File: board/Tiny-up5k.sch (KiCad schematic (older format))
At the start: 37 parts, among them J1 CONN_01X14, J2 CONN_01X14, J5 Prog, SW1 SW_Push, U1 ICE40UP5K-SG48ITR, U2 MIC5504-3.3YM5, U3 DSC6001CI2A-016.0000T, U4 MIC5504-1.2YM5, U5 AT25xxx-MA, U6 USB_OTG

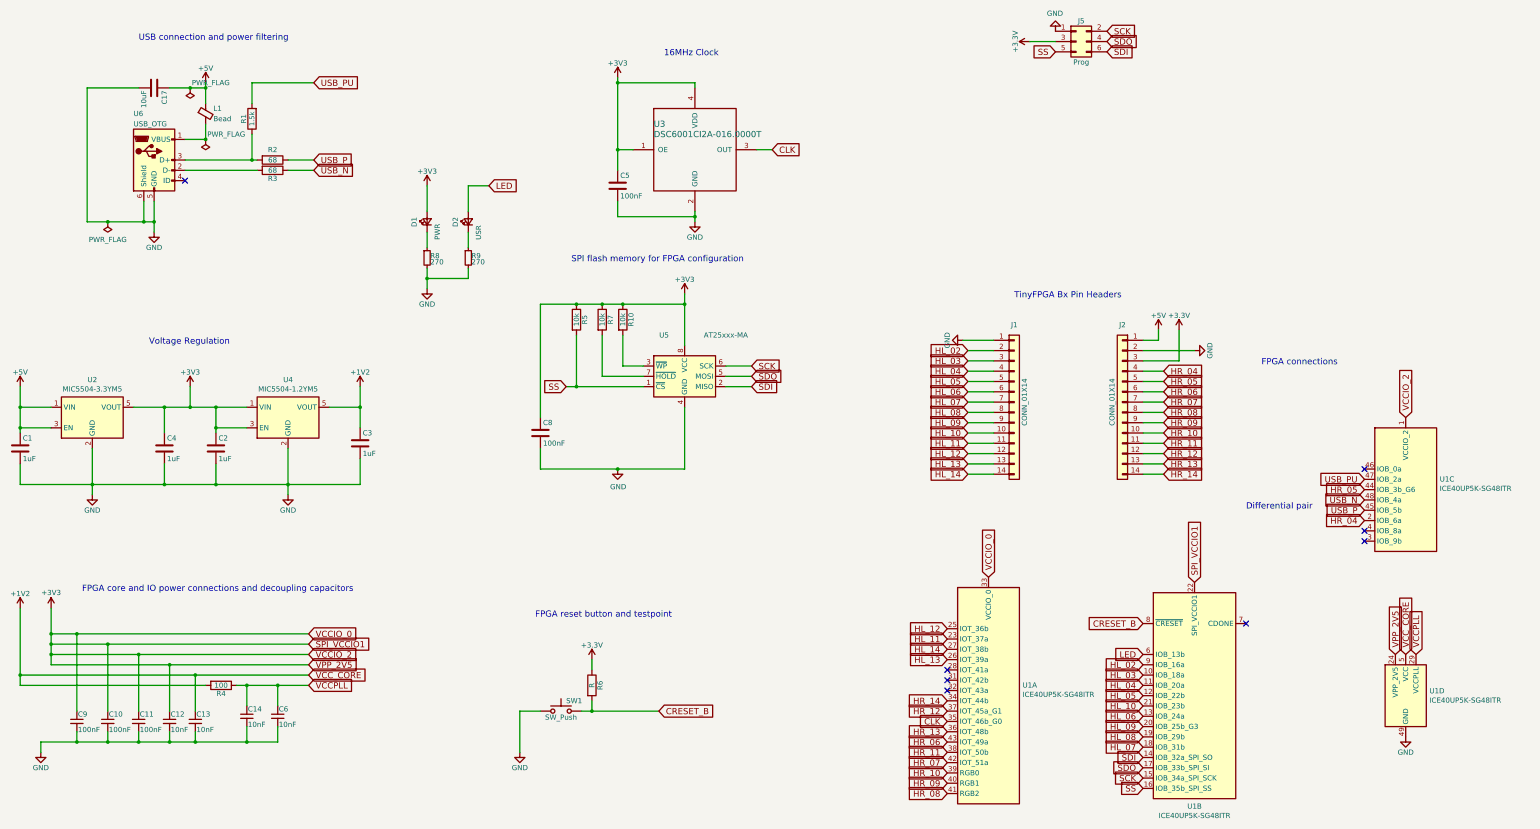
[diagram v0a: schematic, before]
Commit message: Added more part numbers for the components. Changed the footprint of 5v capacitor (make it bigger) to accomodate for the bigger value.
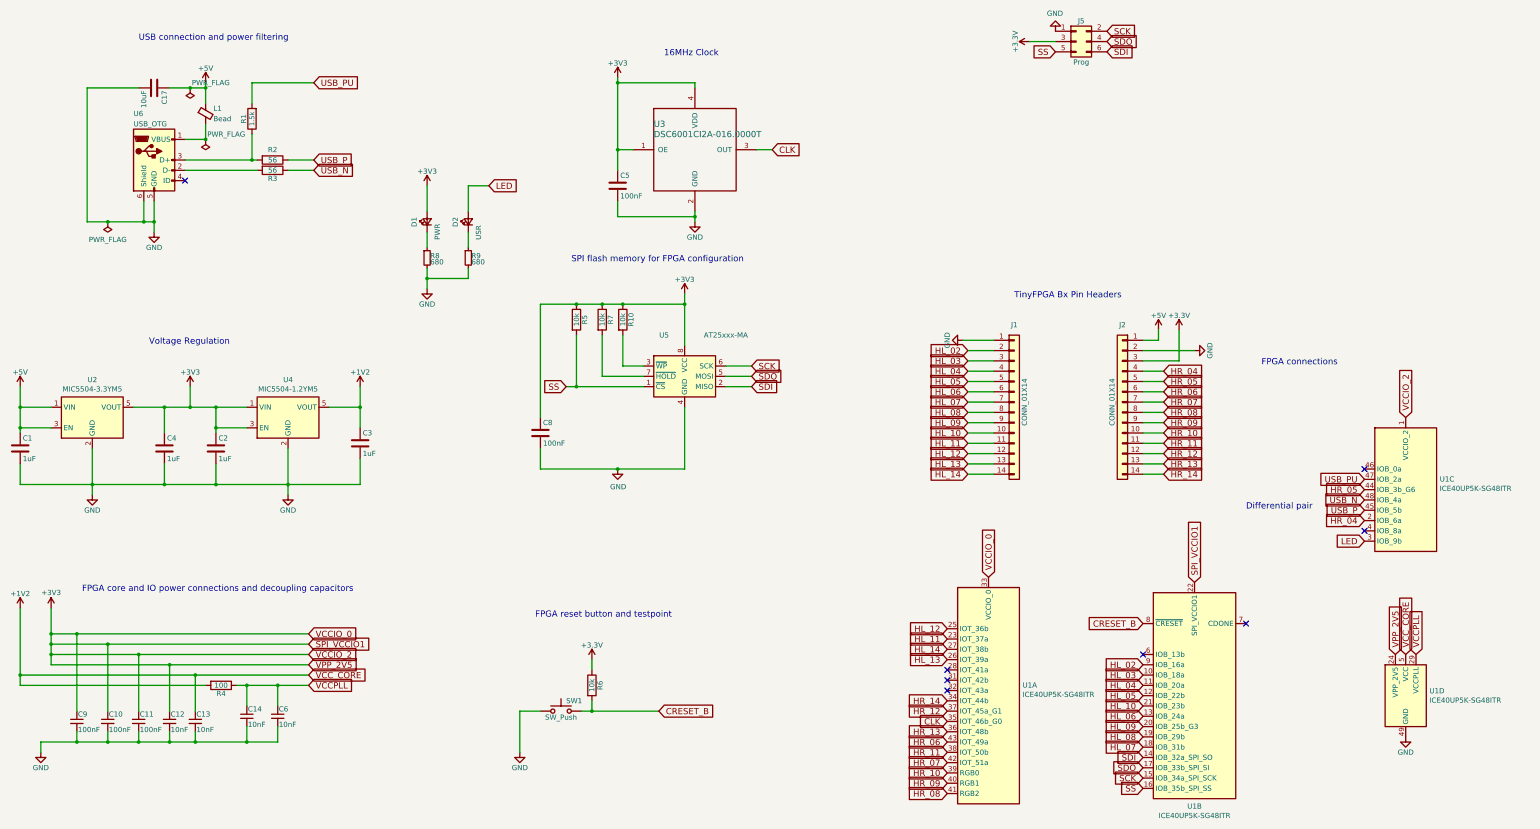
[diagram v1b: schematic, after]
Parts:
- C1, C2, C3, C4: manf# (none) -> GRM155R61A105KE15D
- C10, C11, C5, C8, C9: manf# (none) -> GRM155R71A104KA01D
- C12, C13, C14, C6: manf# (none) -> GRM155R61A103KA01D
- C17: footprint Capacitor_SMD:C_0402_1005Metric -> Capacitor_SMD:C_0603_1608Metric; manf# (none) -> GRM188R61A106KE69D
- D1, D2: manf# (none) -> KPHD-1608LVCGCK
- L1: manf# (none) -> BLM18PG300SN1D
- R1: footprint Resistors_SMD:R_0402_NoSilk -> Resistor_SMD:R_0402_1005Metric; manf# (none) -> CRCW04021K50FKED
- R10, R5, R7: footprint Resistors_SMD:R_0402_NoSilk -> Resistor_SMD:R_0402_1005Metric; manf# (none) -> CRCW040210K0FKED
- R2, R3: value 68 -> 56; footprint Resistors_SMD:R_0402_NoSilk -> Resistor_SMD:R_0402_1005Metric; manf# (none) -> CRCW040256R0FKED
- R4: footprint Resistors_SMD:R_0402_NoSilk -> Resistor_SMD:R_0402_1005Metric; manf# (none) -> CRCW0402100RFKED
- R6: value R -> 10k; footprint Resistors_SMD:R_0402 -> Resistor_SMD:R_0402_1005Metric; manf# (none) -> CRCW040210K0FKED
- R8, R9: value 270 -> 680; footprint Resistors_SMD:R_0402_NoSilk -> Resistor_SMD:R_0402_1005Metric; manf# (none) -> CRCW0402680RFKED
- U2: manf# MIC5504-3.3YM5-TR -> MIC5504-3.3YM5-TR
- U5: #manf AT25SF081-MHD-T -> (none); manf# (none) -> AT25SF081-MHD-T
- U6: manf# USB3076-30-A -> USB3076-30-A
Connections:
- net LED: now also U1.3 (IOB_9b); no longer U1.6 (IOB_13b)
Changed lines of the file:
@@
 encoding utf-8
 Sheet 1 1
-Title "TinyFPGA Bx"
+Title "Tiny-up5k"
 Date ""
 Rev "v1.1"
-Comp "TinyFPGA"
+Comp "Not Organized"
 Comment1 ""
 Comment2 ""
@@
 F 2 "Connector_USB:USB_Micro-B_GCT_USB3076-30-A" H 2350 1950 50  0001 C CNN
 F 3 "" H 2350 1950 50  0001 C CNN
-F 4 "USB3076-30-A " H 2200 2000 50  0001 C CNN "manf#"
+F 4 "USB3076-30-A" H 2200 2000 50  0001 C CNN "manf#"
 	1    2200 2000
 	1    0    0    -1
@@
 F 2 "Capacitor_SMD:C_0402_1005Metric" H 2838 4650 50  0001 C CNN
 F 3 "" H 2800 4800 50  0001 C CNN
+F 4 "GRM155R61A105KE15D" H 0   0   50  0001 C CNN "manf#"
 	1    2800 4800
 	1    0    0    -1
@@
 F 2 "Capacitor_SMD:C_0402_1005Metric" H 4238 4600 50  0001 C CNN
 F 3 "" H 4200 4750 50  0001 C CNN
+F 4 "GRM155R61A105KE15D" H 0   0   50  0001 C CNN "manf#"
 	1    4200 4750
 	1    0    0    -1
@@
 F 2 "Capacitor_SMD:C_0402_1005Metric" H 938 4650 50  0001 C CNN
 F 3 "" H 900 4800 50  0001 C CNN
+F 4 "GRM155R61A105KE15D" H 0   0   50  0001 C CNN "manf#"
 	1    900  4800
 	1    0    0    -1
@@
 F 2 "Capacitor_SMD:C_0402_1005Metric" H 2338 4650 50  0001 C CNN
 F 3 "" H 2300 4800 50  0001 C CNN
+F 4 "GRM155R61A105KE15D" H 0   0   50  0001 C CNN "manf#"
 	1    2300 4800
 	1    0    0    -1
@@
 F 2 "Inductors_SMD:L_0603" V 2630 1550 50  0001 C CNN
 F 3 "" H 2700 1550 50  0001 C CNN
+F 4 "BLM18PG300SN1D" H 2700 1550 50  0001 C CNN "manf#"
 	1    2700 1550
 	1    0    0    -1
@@
 P 3350 2000
 F 0 "R2" V 3250 2000 50  0000 C CNN
-F 1 "68" V 3350 2000 50  0000 C CNN
-F 2 "Resistors_SMD:R_0402_NoSilk" V 3280 2000 50  0001 C CNN
+F 1 "56" V 3350 2000 50  0000 C CNN
+F 2 "Resistor_SMD:R_0402_1005Metric" V 3280 2000 50  0001 C CNN
 F 3 "" H 3350 2000 50  0001 C CNN
+F 4 "CRCW040256R0FKED" H 0   0   50  0001 C CNN "manf#"
 	1    3350 2000
 	0    1    1    0
@@
 P 3350 2100
 F 0 "R3" V 3430 2100 50  0000 C CNN
-F 1 "68" V 3350 2100 50  0000 C CNN
-F 2 "Resistors_SMD:R_0402_NoSilk" V 3280 2100 50  0001 C CNN
+F 1 "56" V 3350 2100 50  0000 C CNN
+F 2 "Resistor_SMD:R_0402_1005Metric" V 3280 2100 50  0001 C CNN
 F 3 "" H 3350 2100 50  0001 C CNN
+F 4 "CRCW040256R0FKED" H 0   0   50  0001 C CNN "manf#"
 	1    3350 2100
 	0    1    1    0
@@
 F 0 "R1" V 3230 1600 50  0000 C CNN
 F 1 "1.5k" V 3150 1600 47  0000 C CNN
-F 2 "Resistors_SMD:R_0402_NoSilk" V 3080 1600 50  0001 C CNN
+F 2 "Resistor_SMD:R_0402_1005Metric" V 3080 1600 50  0001 C CNN
 F 3 "" H 3150 1600 50  0001 C CNN
+F 4 "CRCW04021K50FKED" H 0   0   50  0001 C CNN "manf#"
 	1    3150 1600
 	-1   0    0    1
@@
 F 2 "Capacitor_SMD:C_0402_1005Metric" H 6738 2100 50  0001 C CNN
 F 3 "" H 6700 2250 50  0001 C CNN
+F 4 "GRM155R71A104KA01D" H 0   0   50  0001 C CNN "manf#"
 	1    6700 2250
 	1    0    0    -1
@@
 F 2 "Capacitor_SMD:C_0402_1005Metric" H 5988 4500 50  0001 C CNN
 F 3 "" H 5950 4650 50  0001 C CNN
+F 4 "GRM155R71A104KA01D" H 0   0   50  0001 C CNN "manf#"
 	1    5950 4650
 	1    0    0    -1
@@
 F 2 "Capacitor_SMD:C_0402_1005Metric" H 1450 7450 50  0001 C CNN
 F 3 "" H 1450 7450 50  0001 C CNN
+F 4 "GRM155R71A104KA01D" H 0   0   50  0001 C CNN "manf#"
 	1    1450 7450
 	1    0    0    -1
@@
 F 2 "Capacitor_SMD:C_0402_1005Metric" H 1750 7450 50  0001 C CNN
 F 3 "" H 1750 7450 50  0001 C CNN
+F 4 "GRM155R71A104KA01D" H 0   0   50  0001 C CNN "manf#"
 	1    1750 7450
 	1    0    0    -1
@@
 F 2 "Capacitor_SMD:C_0402_1005Metric" H 2050 7450 50  0001 C CNN
 F 3 "" H 2050 7450 50  0001 C CNN
+F 4 "GRM155R71A104KA01D" H 0   0   50  0001 C CNN "manf#"
 	1    2050 7450
 	1    0    0    -1
@@
 F 2 "Capacitor_SMD:C_0402_1005Metric" H 2350 7450 50  0001 C CNN
 F 3 "" H 2350 7450 50  0001 C CNN
+F 4 "GRM155R61A103KA01D" H 0   0   50  0001 C CNN "manf#"
 	1    2350 7450
 	1    0    0    -1
@@
 F 2 "Capacitor_SMD:C_0402_1005Metric" H 2600 7450 50  0001 C CNN
 F 3 "" H 2600 7450 50  0001 C CNN
+F 4 "GRM155R61A103KA01D" H 0   0   50  0001 C CNN "manf#"
 	1    2600 7450
 	1    0    0    -1
@@
 F 2 "Capacitor_SMD:C_0402_1005Metric" H 3100 7400 50  0001 C CNN
 F 3 "" H 3100 7400 50  0001 C CNN
+F 4 "GRM155R61A103KA01D" H 0   0   50  0001 C CNN "manf#"
 	1    3100 7400
 	1    0    0    -1
@@
 F 0 "R5" V 6380 3550 50  0000 C CNN
 F 1 "10k" V 6300 3550 50  0000 C CNN
-F 2 "Resistors_SMD:R_0402_NoSilk" V 6230 3550 50  0001 C CNN
+F 2 "Resistor_SMD:R_0402_1005Metric" V 6230 3550 50  0001 C CNN
 F 3 "" H 6300 3550 50  0001 C CNN
+F 4 "CRCW040210K0FKED" H 0   0   50  0001 C CNN "manf#"
 	1    6300 3550
 	1    0    0    -1
@@
 P 6450 7100
 F 0 "R6" V 6530 7100 50  0000 C CNN
-F 1 "R" V 6450 7100 50  0000 C CNN
-F 2 "Resistors_SMD:R_0402" V 6380 7100 50  0001 C CNN
+F 1 "10k" V 6450 7100 50  0000 C CNN
+F 2 "Resistor_SMD:R_0402_1005Metric" V 6380 7100 50  0001 C CNN
 F 3 "" H 6450 7100 50  0001 C CNN
+F 4 "CRCW040210K0FKED" H 0   0   50  0001 C CNN "manf#"
 	1    6450 7100
 	1    0    0    -1
@@
 F 0 "C17" H 2225 1400 50  0000 L CNN
 F 1 "10uF" H 2225 1200 50  0000 L CNN
-F 2 "Capacitor_SMD:C_0402_1005Metric" H 2238 1150 50  0001 C CNN
+F 2 "Capacitor_SMD:C_0603_1608Metric" H 2238 1150 50  0001 C CNN
 F 3 "" H 2200 1300 50  0001 C CNN
+F 4 "GRM188R61A106KE69D" H 0   0   50  0001 C CNN "manf#"
 	1    2200 1300
 	0    1    1    0
@@
 F 0 "R7" V 6630 3550 50  0000 C CNN
 F 1 "10k" V 6550 3550 50  0000 C CNN
-F 2 "Resistors_SMD:R_0402_NoSilk" V 6480 3550 50  0001 C CNN
+F 2 "Resistor_SMD:R_0402_1005Metric" V 6480 3550 50  0001 C CNN
 F 3 "" H 6550 3550 50  0001 C CNN
+F 4 "CRCW040210K0FKED" H 0   0   50  0001 C CNN "manf#"
 	1    6550 3550
 	1    0    0    -1
@@
 F 2 "LED_SMD:LED_0402_1005Metric" V 4850 2600 50  0001 C CNN
 F 3 "" V 4850 2600 50  0001 C CNN
+F 4 "KPHD-1608LVCGCK" H 4850 2600 50  0001 C CNN "manf#"
 	1    4850 2600
 	0    -1   -1   0
@@
 F 2 "LED_SMD:LED_0402_1005Metric" V 5250 2600 50  0001 C CNN
 F 3 "" V 5250 2600 50  0001 C CNN
+F 4 "KPHD-1608LVCGCK" H 5250 2600 50  0001 C CNN "manf#"
 	1    5250 2600
 	0    -1   -1   0
@@
 P 4850 2950
 F 0 "R8" H 4880 2970 50  0000 L CNN
-F 1 "270" H 4880 2910 50  0000 L CNN
-F 2 "Resistors_SMD:R_0402_NoSilk" H 4850 2950 50  0001 C CNN
+F 1 "680" H 4880 2910 50  0000 L CNN
+F 2 "Resistor_SMD:R_0402_1005Metric" H 4850 2950 50  0001 C CNN
 F 3 "" H 4850 2950 50  0001 C CNN
+F 4 "CRCW0402680RFKED" H 4850 2950 50  0001 C CNN "manf#"
 	1    4850 2950
 	1    0    0    -1
@@
 P 5250 2950
 F 0 "R9" H 5280 2970 50  0000 L CNN
-F 1 "270" H 5280 2910 50  0000 L CNN
-F 2 "Resistors_SMD:R_0402_NoSilk" H 5250 2950 50  0001 C CNN
+F 1 "680" H 5280 2910 50  0000 L CNN
+F 2 "Resistor_SMD:R_0402_1005Metric" H 5250 2950 50  0001 C CNN
 F 3 "" H 5250 2950 50  0001 C CNN
+F 4 "CRCW0402680RFKED" H 5250 2950 50  0001 C CNN "manf#"
 	1    5250 2950
 	1    0    0    -1
@@
 F 0 "R10" V 6830 3550 50  0000 C CNN
 F 1 "10k" V 6750 3550 50  0000 C CNN
-F 2 "Resistors_SMD:R_0402_NoSilk" V 6680 3550 50  0001 C CNN
+F 2 "Resistor_SMD:R_0402_1005Metric" V 6680 3550 50  0001 C CNN
 F 3 "" H 6750 3550 50  0001 C CNN
+F 4 "CRCW040210K0FKED" H 0   0   50  0001 C CNN "manf#"
 	1    6750 3550
 	1    0    0    -1
@@
 F 0 "R4" V 2930 7100 50  0000 C CNN
 F 1 "100" V 2850 7100 50  0000 C CNN
-F 2 "Resistors_SMD:R_0402_NoSilk" V 2780 7100 50  0001 C CNN
+F 2 "Resistor_SMD:R_0402_1005Metric" V 2780 7100 50  0001 C CNN
 F 3 "" H 2850 7100 50  0001 C CNN
+F 4 "CRCW0402100RFKED" H 0   0   50  0001 C CNN "manf#"
 	1    2850 7100
 	0    1    1    0
@@
 F 2 "Capacitor_SMD:C_0402_1005Metric" H 3400 7400 50  0001 C CNN
 F 3 "" H 3400 7400 50  0001 C CNN
+F 4 "GRM155R61A103KA01D" H 0   0   50  0001 C CNN "manf#"
 	1    3400 7400
 	1    0    0    -1
@@
 Text Notes 12800 5400 0    60   ~ 0
 Differential pair
-Text GLabel 11800 6800 0    60   Input ~ 0
+Text GLabel 13950 5700 0    60   Input ~ 0
 LED
 Text GLabel 11450 750  2    60   Input ~ 0
@@
 F 2 "Package_TO_SOT_SMD:SOT-23-5" H 1600 4100 50  0001 C CNN
 F 3 "http://ww1.microchip.com/downloads/en/DeviceDoc/MIC550X.pdf" H 1350 4750 50  0001 C CNN
-F 4 " MIC5504-3.3YM5-TR" H 1600 4500 50  0001 C CNN "manf#"
+F 4 "MIC5504-3.3YM5-TR" H 1600 4500 50  0001 C CNN "manf#"
 	1    1600 4500
 	1    0    0    -1
@@
 F 2 "Package_DFN_QFN:DFN-8-1EP_3x2mm_P0.5mm_EP1.75x1.45mm" H 7350 4100 50  0001 C CNN
 F 3 "http://ww1.microchip.com/downloads/en/DeviceDoc/Atmel-8707-SEEPROM-AT25010B-020B-040B-Datasheet.pdf" H 7350 4100 50  0001 C CNN
-F 4 "AT25SF081-MHD-T" H 7350 4100 50  0001 C CNN "#manf"
+F 4 "AT25SF081-MHD-T" H 7350 4100 50  0001 C CNN "manf#"
 	1    7350 4100
 	1    0    0    -1
@@
 NoConn ~ 2500 2200
 NoConn ~ 12800 6500
-NoConn ~ 13950 5700
+NoConn ~ 11800 6800
 NoConn ~ 13950 5600
 NoConn ~ 13950 5000

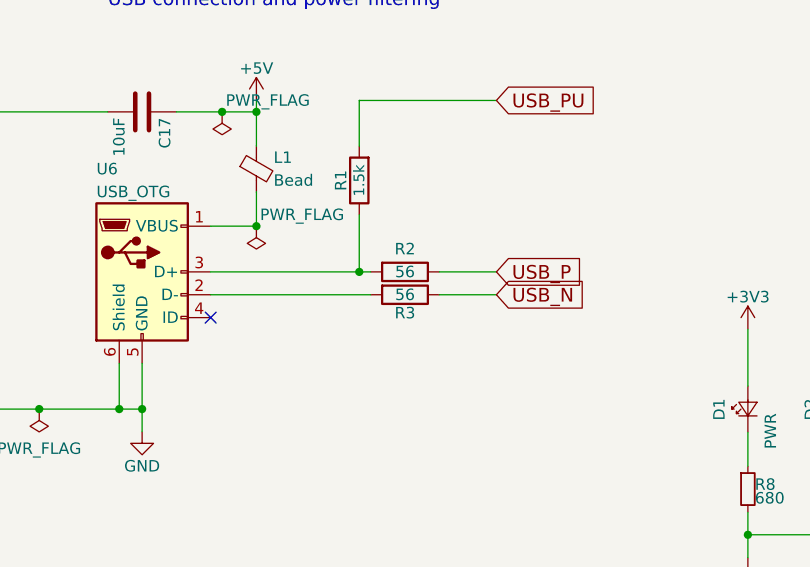
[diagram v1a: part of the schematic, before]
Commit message: Fix spi flash layout size
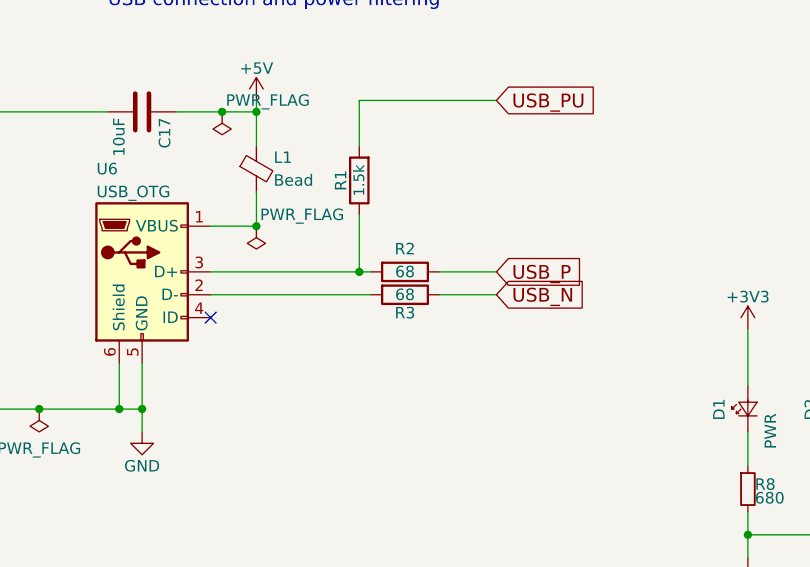
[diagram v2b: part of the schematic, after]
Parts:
- C1, C2, C3, C4: manf# GRM155R61A105KE15D -> CC0402KRX5R6BB105
- C10, C11, C5, C8, C9: manf# GRM155R71A104KA01D -> C0402C104J8RACTU
- C12, C13, C14, C6: manf# GRM155R61A103KA01D -> C0402C103K8RACAUTO
- C17: manf# GRM188R61A106KE69D -> C1608X5R1A106K080AC
- R2, R3: value 56 -> 68
- U5: manf# AT25SF081-MHD-T -> N25Q032A11EF640E
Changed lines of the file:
@@
 F 2 "Capacitor_SMD:C_0402_1005Metric" H 2838 4650 50  0001 C CNN
 F 3 "" H 2800 4800 50  0001 C CNN
-F 4 "GRM155R61A105KE15D" H 0   0   50  0001 C CNN "manf#"
+F 4 "CC0402KRX5R6BB105" H 0   0   50  0001 C CNN "manf#"
 	1    2800 4800
 	1    0    0    -1
@@
 F 2 "Capacitor_SMD:C_0402_1005Metric" H 4238 4600 50  0001 C CNN
 F 3 "" H 4200 4750 50  0001 C CNN
-F 4 "GRM155R61A105KE15D" H 0   0   50  0001 C CNN "manf#"
+F 4 "CC0402KRX5R6BB105" H 0   0   50  0001 C CNN "manf#"
 	1    4200 4750
 	1    0    0    -1
@@
 F 2 "Capacitor_SMD:C_0402_1005Metric" H 938 4650 50  0001 C CNN
 F 3 "" H 900 4800 50  0001 C CNN
-F 4 "GRM155R61A105KE15D" H 0   0   50  0001 C CNN "manf#"
+F 4 "CC0402KRX5R6BB105" H 0   0   50  0001 C CNN "manf#"
 	1    900  4800
 	1    0    0    -1
@@
 F 2 "Capacitor_SMD:C_0402_1005Metric" H 2338 4650 50  0001 C CNN
 F 3 "" H 2300 4800 50  0001 C CNN
-F 4 "GRM155R61A105KE15D" H 0   0   50  0001 C CNN "manf#"
+F 4 "CC0402KRX5R6BB105" H 0   0   50  0001 C CNN "manf#"
 	1    2300 4800
 	1    0    0    -1
@@
 P 3350 2000
 F 0 "R2" V 3250 2000 50  0000 C CNN
-F 1 "56" V 3350 2000 50  0000 C CNN
+F 1 "68" V 3350 2000 50  0000 C CNN
 F 2 "Resistor_SMD:R_0402_1005Metric" V 3280 2000 50  0001 C CNN
 F 3 "" H 3350 2000 50  0001 C CNN
@@
 P 3350 2100
 F 0 "R3" V 3430 2100 50  0000 C CNN
-F 1 "56" V 3350 2100 50  0000 C CNN
+F 1 "68" V 3350 2100 50  0000 C CNN
 F 2 "Resistor_SMD:R_0402_1005Metric" V 3280 2100 50  0001 C CNN
 F 3 "" H 3350 2100 50  0001 C CNN
@@
 F 2 "Capacitor_SMD:C_0402_1005Metric" H 6738 2100 50  0001 C CNN
 F 3 "" H 6700 2250 50  0001 C CNN
-F 4 "GRM155R71A104KA01D" H 0   0   50  0001 C CNN "manf#"
+F 4 "C0402C104J8RACTU" H 0   0   50  0001 C CNN "manf#"
 	1    6700 2250
 	1    0    0    -1
@@
 F 2 "Capacitor_SMD:C_0402_1005Metric" H 5988 4500 50  0001 C CNN
 F 3 "" H 5950 4650 50  0001 C CNN
-F 4 "GRM155R71A104KA01D" H 0   0   50  0001 C CNN "manf#"
+F 4 "C0402C104J8RACTU" H 0   0   50  0001 C CNN "manf#"
 	1    5950 4650
 	1    0    0    -1
@@
 F 2 "Capacitor_SMD:C_0402_1005Metric" H 1450 7450 50  0001 C CNN
 F 3 "" H 1450 7450 50  0001 C CNN
-F 4 "GRM155R71A104KA01D" H 0   0   50  0001 C CNN "manf#"
+F 4 "C0402C104J8RACTU" H 0   0   50  0001 C CNN "manf#"
 	1    1450 7450
 	1    0    0    -1
@@
 F 2 "Capacitor_SMD:C_0402_1005Metric" H 1750 7450 50  0001 C CNN
 F 3 "" H 1750 7450 50  0001 C CNN
-F 4 "GRM155R71A104KA01D" H 0   0   50  0001 C CNN "manf#"
+F 4 "C0402C104J8RACTU" H 0   0   50  0001 C CNN "manf#"
 	1    1750 7450
 	1    0    0    -1
@@
 F 2 "Capacitor_SMD:C_0402_1005Metric" H 2050 7450 50  0001 C CNN
 F 3 "" H 2050 7450 50  0001 C CNN
-F 4 "GRM155R71A104KA01D" H 0   0   50  0001 C CNN "manf#"
+F 4 "C0402C104J8RACTU" H 0   0   50  0001 C CNN "manf#"
 	1    2050 7450
 	1    0    0    -1
@@
 F 2 "Capacitor_SMD:C_0402_1005Metric" H 2350 7450 50  0001 C CNN
 F 3 "" H 2350 7450 50  0001 C CNN
-F 4 "GRM155R61A103KA01D" H 0   0   50  0001 C CNN "manf#"
+F 4 "C0402C103K8RACAUTO" H 0   0   50  0001 C CNN "manf#"
 	1    2350 7450
 	1    0    0    -1
@@
 F 2 "Capacitor_SMD:C_0402_1005Metric" H 2600 7450 50  0001 C CNN
 F 3 "" H 2600 7450 50  0001 C CNN
-F 4 "GRM155R61A103KA01D" H 0   0   50  0001 C CNN "manf#"
+F 4 "C0402C103K8RACAUTO" H 0   0   50  0001 C CNN "manf#"
 	1    2600 7450
 	1    0    0    -1
@@
 F 2 "Capacitor_SMD:C_0402_1005Metric" H 3100 7400 50  0001 C CNN
 F 3 "" H 3100 7400 50  0001 C CNN
-F 4 "GRM155R61A103KA01D" H 0   0   50  0001 C CNN "manf#"
+F 4 "C0402C103K8RACAUTO" H 0   0   50  0001 C CNN "manf#"
 	1    3100 7400
 	1    0    0    -1
@@
 F 2 "Capacitor_SMD:C_0603_1608Metric" H 2238 1150 50  0001 C CNN
 F 3 "" H 2200 1300 50  0001 C CNN
-F 4 "GRM188R61A106KE69D" H 0   0   50  0001 C CNN "manf#"
+F 4 "C1608X5R1A106K080AC" H 0   0   50  0001 C CNN "manf#"
 	1    2200 1300
 	0    1    1    0
@@
 F 2 "Capacitor_SMD:C_0402_1005Metric" H 3400 7400 50  0001 C CNN
 F 3 "" H 3400 7400 50  0001 C CNN
-F 4 "GRM155R61A103KA01D" H 0   0   50  0001 C CNN "manf#"
+F 4 "C0402C103K8RACAUTO" H 0   0   50  0001 C CNN "manf#"
 	1    3400 7400
 	1    0    0    -1
@@
 F 2 "Package_DFN_QFN:DFN-8-1EP_3x2mm_P0.5mm_EP1.75x1.45mm" H 7350 4100 50  0001 C CNN
 F 3 "http://ww1.microchip.com/downloads/en/DeviceDoc/Atmel-8707-SEEPROM-AT25010B-020B-040B-Datasheet.pdf" H 7350 4100 50  0001 C CNN
-F 4 "AT25SF081-MHD-T" H 7350 4100 50  0001 C CNN "manf#"
+F 4 "N25Q032A11EF640E" H 7350 4100 50  0001 C CNN "manf#"
 	1    7350 4100
 	1    0    0    -1

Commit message: Increase the spacing between the leds and their resistor.
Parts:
- U5: manf# N25Q032A11EF640E -> SST25VF016B-50-4C-QAF-T
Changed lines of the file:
@@
 F 2 "Package_DFN_QFN:DFN-8-1EP_3x2mm_P0.5mm_EP1.75x1.45mm" H 7350 4100 50  0001 C CNN
 F 3 "http://ww1.microchip.com/downloads/en/DeviceDoc/Atmel-8707-SEEPROM-AT25010B-020B-040B-Datasheet.pdf" H 7350 4100 50  0001 C CNN
-F 4 "N25Q032A11EF640E" H 7350 4100 50  0001 C CNN "manf#"
+F 4 " SST25VF016B-50-4C-QAF-T" H 7350 4100 50  0001 C CNN "manf#"
 	1    7350 4100
 	1    0    0    -1
